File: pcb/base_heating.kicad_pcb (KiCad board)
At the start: 2 copper layers, 65 x 65.1 mm, 80 parts, among them J1 X1_1-20, J10 I2C, J11 USB, J12 POWER_BUS, J13 POWER_BUS, J14 DCSW_2, J15 DCSW_1, J16 ACSW_1, J17 RS422, J2 X1_21-40, J3 STEPDOWN, J4 BOOT, J5 GND, J6 DIN_1, J7 SWD, J8 I2C, J9 A_D_IN, Q1 NTR2101P, Q2 IRF540N, Q3 IRF540N, Q4 IRF540N, Q5 IRF540N, Q6 BT136, U1 MAX3078E, U2 SN65HVD230, U3 AT24CS64-SSHM, U4 STM32F072C8Tx, U5 MOC3061M, U6 MOC3061M

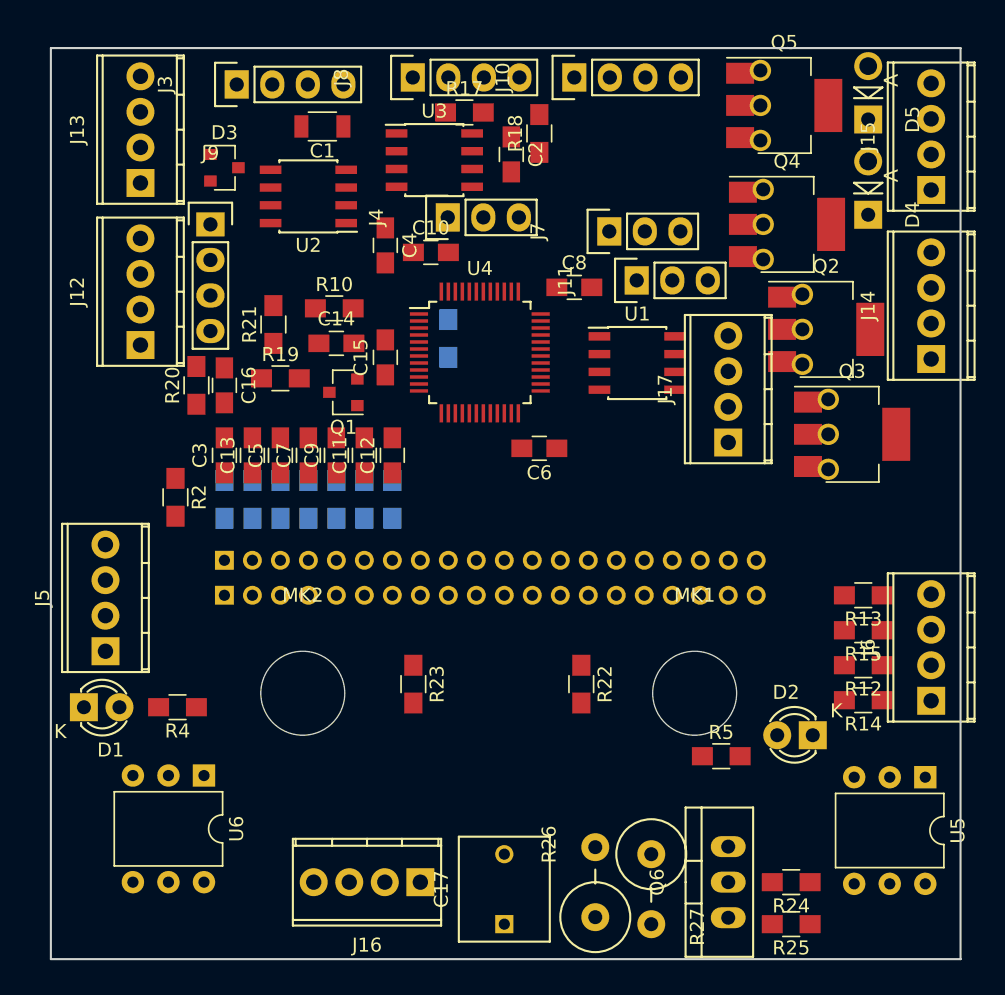
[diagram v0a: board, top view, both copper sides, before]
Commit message: Finished schematics, updated screenshot
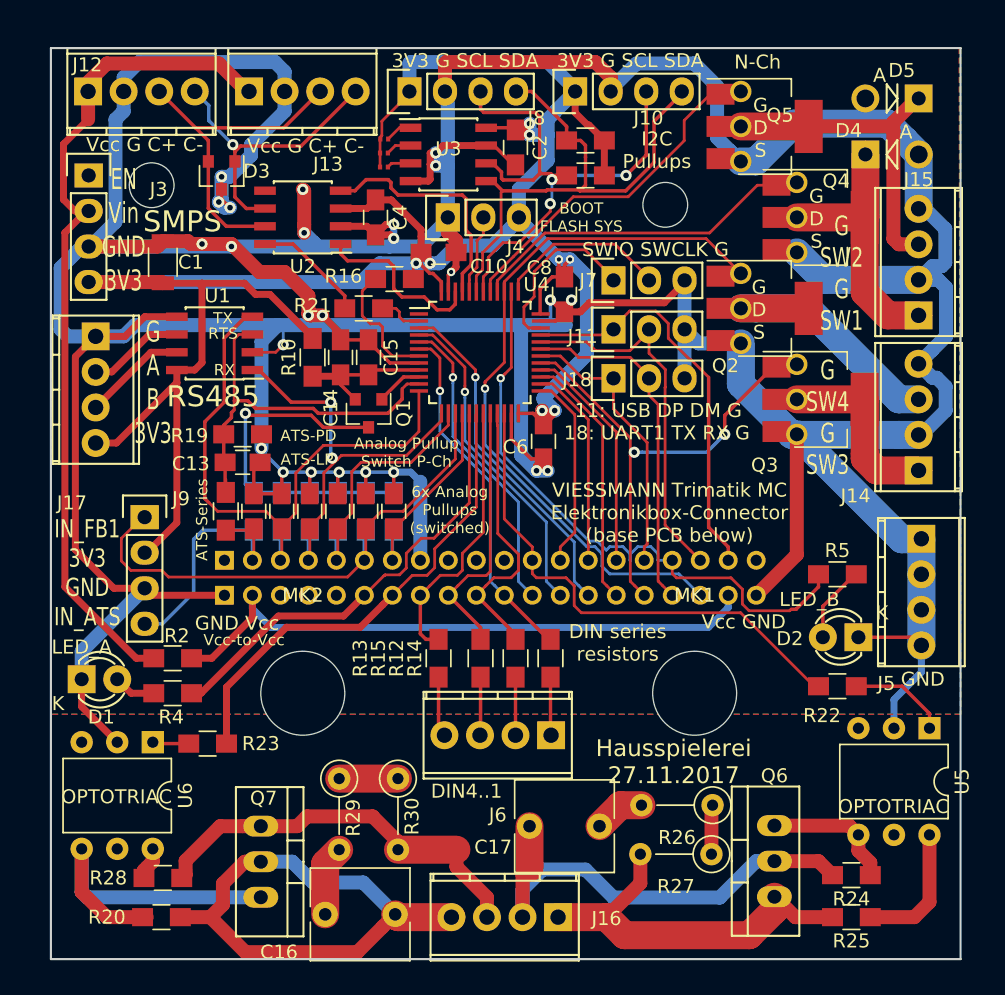
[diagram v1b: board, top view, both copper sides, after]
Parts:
- added J18: UART_1, Pin_Headers:Pin_Header_Straight_1x03, F.Cu at (71.5, 52.0)
- added JP1: Jumper_NO_Small, Capacitors_SMD:C_0201_NoSilk, F.Cu at (55.1, 36.9)
- added JP2: Jumper_NO_Small, Capacitors_SMD:C_0201_NoSilk, F.Cu at (55.1, 35.9)
- added JP3: Jumper_NO_Small, Capacitors_SMD:C_0201_NoSilk, F.Cu at (55.1, 34.9)
- added Q7: BT136, TO_SOT_Packages_THT:TO-220_Neutral123_Vertical, F.Cu at (46.3, 86.5)
- added R28: 360, Resistors_SMD:R_0805_HandSoldering, F.Cu at (39.3, 87.7)
- added R29: 38, Resistors_THT:R_Axial_DIN0207_L6.3mm_D2.5mm_P5.08mm_Vertical, F.Cu at (51.9, 80.6)
- added R30: 38, Resistors_THT:R_Axial_DIN0207_L6.3mm_D2.5mm_P5.08mm_Vertical, F.Cu at (56.1, 80.6)
- added REF**: MountingHole_3.2mm_M3, Mounting_Holes:MountingHole_3.2mm_M3, F.Cu at (75.2, 39.6)
- added REF**: MountingHole_3.2mm_M3, Mounting_Holes:MountingHole_3.2mm_M3, F.Cu at (38.5, 38.2)
- C16: value 100n -> 10n; footprint Capacitors_SMD:C_0805_HandSoldering -> Capacitors_THT:C_Rect_L7.0mm_W6.5mm_P5.00mm
- C17: footprint Capacitors_ThroughHole:C_Rect_L7.5_W6.5_P5 -> Capacitors_THT:C_Rect_L7.0mm_W6.5mm_P5.00mm
- R16, R7: moved to F.Cu
- R19: value 0 -> 10k
- R20: value 10k -> 360
- R26, R27: footprint Resistors_ThroughHole:Resistor_Vertical_RM5mm -> Resistors_THT:R_Axial_DIN0207_L6.3mm_D2.5mm_P5.08mm_Vertical
- moved J5 58.9 mm to (93.5, 63.5), turned to 270 degrees
- moved J17 45.8 mm to (34.5, 49.0), turned to 270 degrees
- moved C16 39.7 mm to (55.9, 90.3), turned to 180 degrees
- moved R20 38.1 mm to (39.2, 90.5), turned to 0 degrees
- moved R13 30.7 mm to (59.0, 72.0), turned to 90 degrees
- moved U1 30.2 mm to (43.0, 49.5), turned to 180 degrees
- moved R15 27.4 mm to (62.0, 72.0), turned to 90 degrees
- moved J6 27.3 mm to (67.0, 77.5), turned to 180 degrees
- moved R12 24.9 mm to (64.5, 72.0), turned to 90 degrees
- moved R14 22.6 mm to (67.0, 72.0), turned to 90 degrees
- moved J9 21.4 mm to (38.0, 61.9)
- moved J12 18.5 mm to (34.0, 31.5), turned to 0 degrees
- moved R22 18.3 mm to (87.5, 74.0), turned to 0 degrees
- moved R5 15.4 mm to (87.5, 66.0)
- moved R23 15.3 mm to (42.5, 78.1), turned to 180 degrees
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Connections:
- C16 pad 2: GND -> Net-(C16-Pad2)
- C3 pad 1: Net-(C3-Pad1) -> AIN_A_D
- J1 pad 12: (no net) -> ACSW_1
- J1 pad 13: (no net) -> DOUT_SW_UKN
- J1 pad 14: (no net) -> DOUT_K3_21
- J1 pad 15: (no net) -> DOUT_K5_S3
- J1 pad 16: (no net) -> DOUT_K4_T2
- J1 pad 17: (no net) -> DOUT_K6_20B
- J1 pad 18: (no net) -> DOUT_K2_20A
- J1 pad 19: (no net) -> DOUT_K1_FIRE
- J1 pad 2: Net-(C3-Pad1) -> AIN_A_D
- J11 pad 1: USB_DP -> DOUT_K1_FIRE
- J11 pad 2: USB_DM -> DOUT_K2_20A
- J16 pad 4: Net-(J16-Pad4) -> Net-(C16-Pad1)
- J17 pad 4: (no net) -> +3V3
- J2 pad 10: (no net) -> DIN2
- J2 pad 11: (no net) -> DIN1
- J2 pad 12: (no net) -> DIN_SW_B2_246
- J2 pad 13: (no net) -> DIN_SW_B1_246
- J2 pad 14: (no net) -> DIN_SW_B0_246
- J2 pad 15: (no net) -> DIN_SW_B0_135
- J2 pad 16: (no net) -> DIN_SW_B1_135
- J2 pad 17: (no net) -> DIN_SW_B2_135
- J2 pad 18: (no net) -> DIN_SW_B3_135
- J2 pad 6: (no net) -> DOUT_LED_RED
- J2 pad 7: (no net) -> ACSW_2
- J2 pad 8: (no net) -> DIN4
- J2 pad 9: (no net) -> DIN3
- J9 pad 1: (no net) -> AIN_FB1
- J9 pad 4: Net-(C16-Pad1) -> AIN_A_D
- Q2 pad 1: ODSW_4 -> DIN_SW_B3_135
- Q3 pad 1: ODSW_3 -> DIN_SW_B1_135
- R1 pad 2: Net-(C3-Pad1) -> AIN_A_D
- R12 pad 2: (no net) -> DIN2
- R13 pad 2: (no net) -> DIN4
- R14 pad 2: (no net) -> DIN1
- R15 pad 2: (no net) -> DIN3
- R19 pad 1: Net-(C16-Pad1) -> GND
- R19 pad 2: AIN_A_D -> AIN_ATS
- R20 pad 1: GND -> Net-(Q7-Pad3)
- R21 pad 1: (no net) -> CAN_SUSPEND
- R22 pad 1: (no net) -> ACSW_1
- R23 pad 1: (no net) -> ACSW_2
- R4 pad 1: (no net) -> DOUT_LED_RED
- R5 pad 1: (no net) -> DOUT_K6_20B
- R7 pad 2: Net-(C3-Pad1) -> AIN_A_D
- U1 pad 1: RS422RX -> AIN_VTS
- U1 pad 2: (no net) -> GND
- U1 pad 3: (no net) -> AIN_ATS
- U1 pad 4: RS422TX -> AIN_KTS
- U3 pad 1: GND -> Net-(JP3-Pad2)
- U3 pad 2: GND -> Net-(JP2-Pad2)
- U3 pad 3: GND -> Net-(JP1-Pad2)
- U4 pad 17: AIN_A_D -> DOUT_LED_RED
- U4 pad 18: (no net) -> ACSW_2
- U4 pad 19: (no net) -> DIN4
- U4 pad 2: (no net) -> CAN_SUSPEND
- U4 pad 20: (no net) -> DIN3
- U4 pad 21: (no net) -> DIN2
- U4 pad 22: (no net) -> ACSW_1
- U4 pad 25: (no net) -> DOUT_SW_UKN
- U4 pad 26: (no net) -> DOUT_K3_21
- U4 pad 27: (no net) -> DIN_SW_B0_135
- U4 pad 28: (no net) -> DOUT_K5_S3
- U4 pad 29: (no net) -> DIN_SW_B1_135
- U4 pad 3: (no net) -> DIN_SW_B0_246
- U4 pad 30: RS422TX -> DOUT_K4_T2
- U4 pad 31: RS422RX -> DIN_SW_B2_135
- U4 pad 32: USB_DM -> DOUT_K2_20A
- U4 pad 33: USB_DP -> DOUT_K1_FIRE
- U4 pad 38: (no net) -> DOUT_K6_20B
- U4 pad 39: (no net) -> DIN_SW_B3_135
- U4 pad 4: (no net) -> DIN_SW_B1_246
- U4 pad 40: (no net) -> ODSW_1
- U4 pad 41: (no net) -> ODSW_2
- U4 pad 5: (no net) -> DIN_SW_B2_246
- U4 pad 6: (no net) -> DIN1
- U6 pad 4: Net-(J16-Pad4) -> Net-(Q7-Pad3)
- U6 pad 6: Net-(J16-Pad3) -> Net-(R28-Pad2)
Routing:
- net GND: track 0.00 -> 475.5 mm, vias 0 -> 25
- net +3V3: track 0.00 -> 172.2 mm, vias 0 -> 8
- net +24V: track 0.00 -> 60.3 mm
- net DIN_SW_B3_135: track 0.00 -> 53.3 mm, vias 0 -> 1
- net VCC_18: track 0.00 -> 44.1 mm
- net DOUT_K6_20B: track 0.00 -> 43.8 mm, vias 0 -> 1
- net AIN_KTS: track 0.00 -> 43.5 mm
- net SCL: track 0.00 -> 40.4 mm, vias 0 -> 3
- net Net-(C16-Pad1): track 0.00 -> 38.6 mm
- net AIN_FB1: track 0.00 -> 38.5 mm
- net SDA: track 0.00 -> 37.6 mm
- net ACSW_1: track 0.00 -> 36.9 mm
- net DIN_SW_B1_135: track 0.00 -> 35.7 mm, vias 0 -> 2
- net ACSW_2: track 0.00 -> 34.7 mm
- net Net-(C17-Pad1): track 0.00 -> 33.7 mm
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- added copper zone on B.Cu, net GND
- added copper zone on F.Cu, net GND
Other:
- net class Default: trace_width 0.25 -> 0.15; via_drill 0.4 -> 0.3
- rule pad_to_mask_clearance: 0.2 -> 0.14
- rule trace_min: 0.2 -> 0.15
- rule via_min_size: 0.4 -> 0.6
- board text added: "11: USB DP DM G"
- board text added: "18: UART1 TX RX G"
- board text added: "3V3 G SCL SDA"
- board text added: "6x Analog Lowpass-C"
- board text added: "6x Analog Pullups (switched)"
- board text added: "ATS-LP"
- board text added: "ATS-PD"
- board text added: "ATS-Series"
- board text added: "Analog Pullup Switch P-Ch"
- board text added: "BOOT FLASH SYS"
- board text added: "DIN series resistors"
- board text added: "DIN4..1"
- board text added: "EN Vin GND 3V3"
- board text added: "G A B 3V3"
- board text added: "G D S"
- board text added: "G SW2 G SW1"
- board text added: "G SW4 G SW3"
- board text added: "GND"
- board text added: "GND Vcc"
- board text added: "Hausspielerei 27.11.2017"
- board text added: "I2C Pullups"
- board text added: "IN_FB1 3V3 GND IN_ATS"
- board text added: "LED_A"
- board text added: "LED_B"
- board text added: "N-Ch"
- board text added: "OPTOTRIAC"
- board text added: "RS485"
- board text added: "RTS"
- board text added: "RX"
- board text added: "SMPS"
- board text added: "SWIO SWCLK G"
- board text added: "TX"
- board text added: "VIESSMANN Trimatik MC Elektronikbox-Connector (base PCB below)"
- board text added: "Vcc G C+ C-"
- board text added: "Vcc GND"
- board text added: "Vcc-to-Vcc"
